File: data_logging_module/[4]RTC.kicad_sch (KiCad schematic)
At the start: 10 parts, among them U1 PCF8563TS, Y1 32768Hz

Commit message: Initial scheme
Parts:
- renumbered BT1 to BT400, C2 to C400, C3 to C401, C1 to C402, D1 to D400, D2 to D401, R1 to R400, R2 to R401, U1 to U400, Y1 to Y400
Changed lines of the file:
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@@
 	(wire
 		(pts
-			(xy 105.41 73.66) (xy 111.76 73.66)
+			(xy 105.41 73.66) (xy 120.65 73.66)
 		)
 		(stroke
@@
 	(wire
 		(pts
-			(xy 83.82 83.82) (xy 111.76 83.82)
+			(xy 83.82 83.82) (xy 120.65 83.82)
 		)
 		(stroke
@@
 	(wire
 		(pts
-			(xy 96.52 76.2) (xy 111.76 76.2)
+			(xy 96.52 76.2) (xy 120.65 76.2)
 		)
 		(stroke
@@
 	(global_label "I2C_SDA"
 		(shape input)
-		(at 111.76 76.2 0)
+		(at 120.65 76.2 0)
 		(fields_autoplaced yes)
 		(effects
@@
 		)
 		(property "Intersheetrefs" "${INTERSHEET_REFS}"
-			(at 122.3652 76.2 0)
+			(at 131.2552 76.2 0)
 			(effects
 				(font
@@
 	(global_label "I2C_SCL"
 		(shape input)
-		(at 111.76 73.66 0)
+		(at 120.65 73.66 0)
 		(fields_autoplaced yes)
 		(effects
@@
 		)
 		(property "Intersheetrefs" "${INTERSHEET_REFS}"
-			(at 122.3047 73.66 0)
+			(at 131.1947 73.66 0)
 			(effects
 				(font
@@
 	(global_label "PCF8563_INT"
 		(shape input)
-		(at 111.76 83.82 0)
+		(at 120.65 83.82 0)
 		(fields_autoplaced yes)
 		(effects
@@
 		)
 		(property "Intersheetrefs" "${INTERSHEET_REFS}"
-			(at 127.0823 83.82 0)
+			(at 135.9723 83.82 0)
 			(effects
 				(font
@@
 		(dnp no)
 		(fields_autoplaced yes)
-		(property "Reference" "U1"
+		(property "Reference" "U400"
 			(at 75.8541 66.04 0)
 			(effects
@@
 			(project "data_logging_module"
 				(path "/e3d8fa9d-8b66-405e-a340-c0b2170fd0cf/c174b425-f1e9-49e9-9571-9bedff230a92"
-					(reference "U1")
+					(reference "U400")
 					(unit 1)
 				)
@@
 		(dnp no)
 		(fields_autoplaced yes)
-		(property "Reference" "R1"
+		(property "Reference" "R400"
 			(at 99.06 63.4999 0)
 			(effects
@@
 			(project "data_logging_module"
 				(path "/e3d8fa9d-8b66-405e-a340-c0b2170fd0cf/c174b425-f1e9-49e9-9571-9bedff230a92"
-					(reference "R1")
+					(reference "R400")
 					(unit 1)
 				)
@@
 		(dnp no)
 		(fields_autoplaced yes)
-		(property "Reference" "D1"
+		(property "Reference" "D400"
 			(at 67.31 53.34 0)
 			(effects
@@
 			(project "data_logging_module"
 				(path "/e3d8fa9d-8b66-405e-a340-c0b2170fd0cf/c174b425-f1e9-49e9-9571-9bedff230a92"
-					(reference "D1")
+					(reference "D400")
 					(unit 1)
 				)
@@
 		(dnp no)
 		(fields_autoplaced yes)
-		(property "Reference" "R2"
+		(property "Reference" "R401"
 			(at 107.95 63.4999 0)
 			(effects
@@
 			(project "data_logging_module"
 				(path "/e3d8fa9d-8b66-405e-a340-c0b2170fd0cf/c174b425-f1e9-49e9-9571-9bedff230a92"
-					(reference "R2")
+					(reference "R401")
 					(unit 1)
 				)
@@
 		(on_board yes)
 		(dnp no)
-		(property "Reference" "Y1"
+		(property "Reference" "Y400"
 			(at 52.832 82.55 0)
 			(effects
@@
 			(project "data_logging_module"
 				(path "/e3d8fa9d-8b66-405e-a340-c0b2170fd0cf/c174b425-f1e9-49e9-9571-9bedff230a92"
-					(reference "Y1")
+					(reference "Y400")
 					(unit 1)
 				)
@@
 		(dnp no)
 		(fields_autoplaced yes)
-		(property "Reference" "C2"
+		(property "Reference" "C400"
 			(at 107.95 34.2899 0)
 			(effects
@@
 			(project "data_logging_module"
 				(path "/e3d8fa9d-8b66-405e-a340-c0b2170fd0cf/c174b425-f1e9-49e9-9571-9bedff230a92"
-					(reference "C2")
+					(reference "C400")
 					(unit 1)
 				)
@@
 		(dnp no)
 		(fields_autoplaced yes)
-		(property "Reference" "C3"
+		(property "Reference" "C401"
 			(at 120.65 34.2899 0)
 			(effects
@@
 			(project "data_logging_module"
 				(path "/e3d8fa9d-8b66-405e-a340-c0b2170fd0cf/c174b425-f1e9-49e9-9571-9bedff230a92"
-					(reference "C3")
+					(reference "C401")
 					(unit 1)
 				)
@@
 		(on_board yes)
 		(dnp no)
-		(property "Reference" "C1"
+		(property "Reference" "C402"
 			(at 38.862 90.17 0)
 			(effects
@@
 			(project "data_logging_module"
 				(path "/e3d8fa9d-8b66-405e-a340-c0b2170fd0cf/c174b425-f1e9-49e9-9571-9bedff230a92"
-					(reference "C1")
+					(reference "C402")
 					(unit 1)
 				)
@@
 		(dnp no)
 		(fields_autoplaced yes)
-		(property "Reference" "D2"
+		(property "Reference" "D401"
 			(at 80.01 53.34 0)
 			(effects
@@
 			(project "data_logging_module"
 				(path "/e3d8fa9d-8b66-405e-a340-c0b2170fd0cf/c174b425-f1e9-49e9-9571-9bedff230a92"
-					(reference "D2")
+					(reference "D401")
 					(unit 1)
 				)
@@
 		(dnp no)
 		(fields_autoplaced yes)
-		(property "Reference" "BT1"
+		(property "Reference" "BT400"
 			(at 43.5229 52.07 0)
 			(effects
@@
 			(project "data_logging_module"
 				(path "/e3d8fa9d-8b66-405e-a340-c0b2170fd0cf/c174b425-f1e9-49e9-9571-9bedff230a92"
-					(reference "BT1")
+					(reference "BT400")
 					(unit 1)
 				)

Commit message: BOM updates
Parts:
- BT400: footprint esp32s3_watches:MPD_BC2032-E2 -> data_logging_module:MPD_BC2032-E2; Manufacturer Part Number (none) -> BS-02-A1AJ010
- C400: Manufacturer Part Number (none) -> CL21A106KOQNNNE
- C401: Manufacturer Part Number (none) -> CL10B104KB8NNNC
- C402: Manufacturer Part Number (none) -> CL10C150JB8NNNC
- D400, D401: Manufacturer Part Number (none) -> 1N4148W
- R400, R401: Manufacturer Part Number (none) -> 0805W8F5101T5E
- U400: Manufacturer Part Number (none) -> PCF8563TS/5,118
- Y400: Manufacturer Part Number (none) -> OK2EL89CJI-111YLC-32.768K
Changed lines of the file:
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@@
+			)
+		)
+		(property "Manufacturer Part Number" "PCF8563TS/5,118"
+			(at 73.66 78.74 0)
+			(effects
+				(font
+					(size 1.27 1.27)
+				)
+				(hide yes)
 			)
 		)
@@
 			)
 		)
+		(property "Manufacturer Part Number" "0805W8F5101T5E"
+			(at 96.52 64.77 0)
+			(effects
+				(font
+					(size 1.27 1.27)
+				)
+				(hide yes)
+			)
+		)
 		(pin "2"
 		)
@@
 			)
 		)
+		(property "Manufacturer Part Number" "1N4148W"
+			(at 67.31 59.69 0)
+			(effects
+				(font
+					(size 1.27 1.27)
+				)
+				(hide yes)
+			)
+		)
 		(pin "2"
 		)
@@
 			)
 		)
+		(property "Manufacturer Part Number" "0805W8F5101T5E"
+			(at 105.41 64.77 0)
+			(effects
+				(font
+					(size 1.27 1.27)
+				)
+				(hide yes)
+			)
+		)
 		(pin "2"
 		)
@@
 		)
 		(property "Manufacturer Product Number" "OK2EL89CJI-111YLC-32.768K"
+			(at 50.8 87.63 0)
+			(effects
+				(font
+					(size 1.27 1.27)
+				)
+				(hide yes)
+			)
+		)
+		(property "Manufacturer Part Number" "OK2EL89CJI-111YLC-32.768K"
 			(at 50.8 87.63 0)
 			(effects
@@
 			)
 		)
+		(property "Manufacturer Part Number" "CL21A106KOQNNNE"
+			(at 104.14 35.56 0)
+			(effects
+				(font
+					(size 1.27 1.27)
+				)
+				(hide yes)
+			)
+		)
 		(pin "2"
 		)
@@
 			)
 		)
+		(property "Manufacturer Part Number" "CL10B104KB8NNNC"
+			(at 116.84 35.56 0)
+			(effects
+				(font
+					(size 1.27 1.27)
+				)
+				(hide yes)
+			)
+		)
 		(pin "2"
 		)
@@
 		)
 		(property "Manufacturer Product Number" "CL10C150JB8NNNC"
+			(at 38.1 92.71 0)
+			(effects
+				(font
+					(size 1.27 1.27)
+				)
+				(hide yes)
+			)
+		)
+		(property "Manufacturer Part Number" "CL10C150JB8NNNC"
 			(at 38.1 92.71 0)
 			(effects
@@
 			)
 		)
+		(property "Manufacturer Part Number" "1N4148W"
+			(at 80.01 59.69 0)
+			(effects
+				(font
+					(size 1.27 1.27)
+				)
+				(hide yes)
+			)
+		)
 		(pin "2"
 		)
@@
 			)
 		)
-		(property "Footprint" "esp32s3_watches:MPD_BC2032-E2"
+		(property "Footprint" "data_logging_module:MPD_BC2032-E2"
 			(at 43.18 59.69 0)
 			(effects
@@
 			(at 43.18 59.69 0)
 			(effects
+				(font
+					(size 1.27 1.27)
+				)
+				(hide yes)
+			)
+		)
+		(property "Manufacturer Part Number" "BS-02-A1AJ010"
+			(at 43.18 59.69 0)
+			(effects

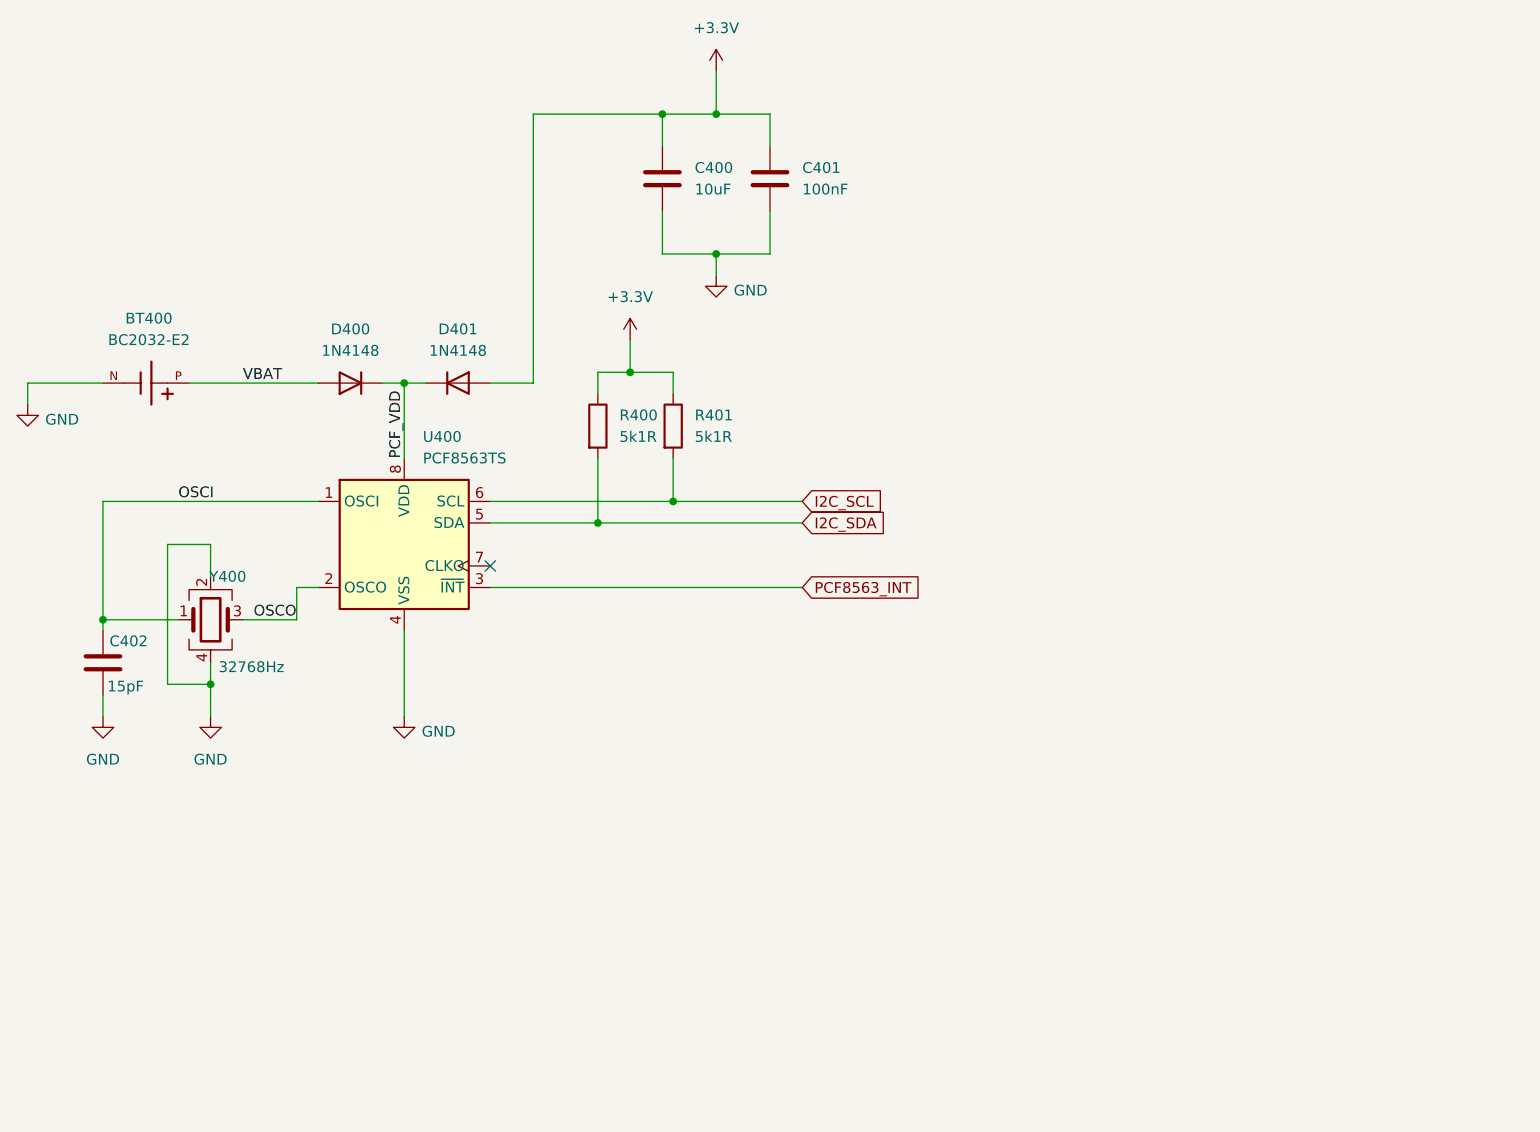
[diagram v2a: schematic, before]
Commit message: Add scheme plots
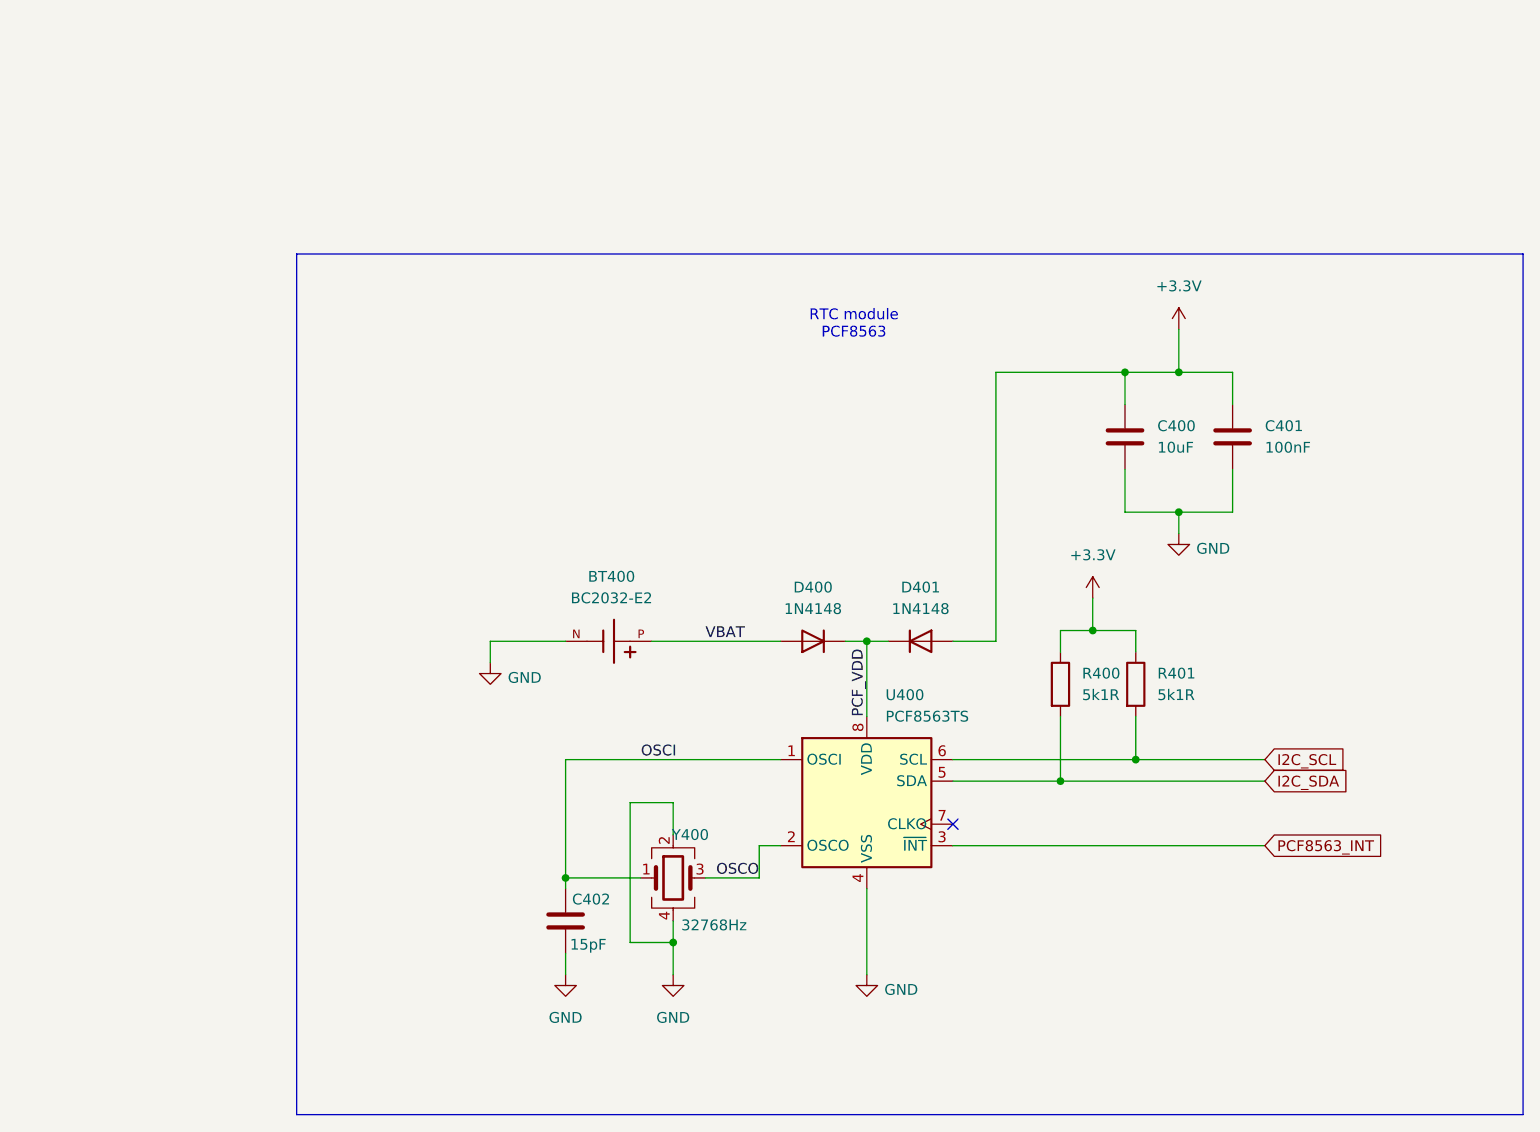
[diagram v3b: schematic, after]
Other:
- note added: "RTC module PCF8563"
- moved on the sheet: BT400, C400, C401, C402, D400, D401, R400, R401, U400, Y400
